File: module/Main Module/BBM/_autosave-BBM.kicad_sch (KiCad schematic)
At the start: 27 parts, among them Q1 NPN, Q2 BS250, Q3 BS170, SW1 SW_DPDT_x2

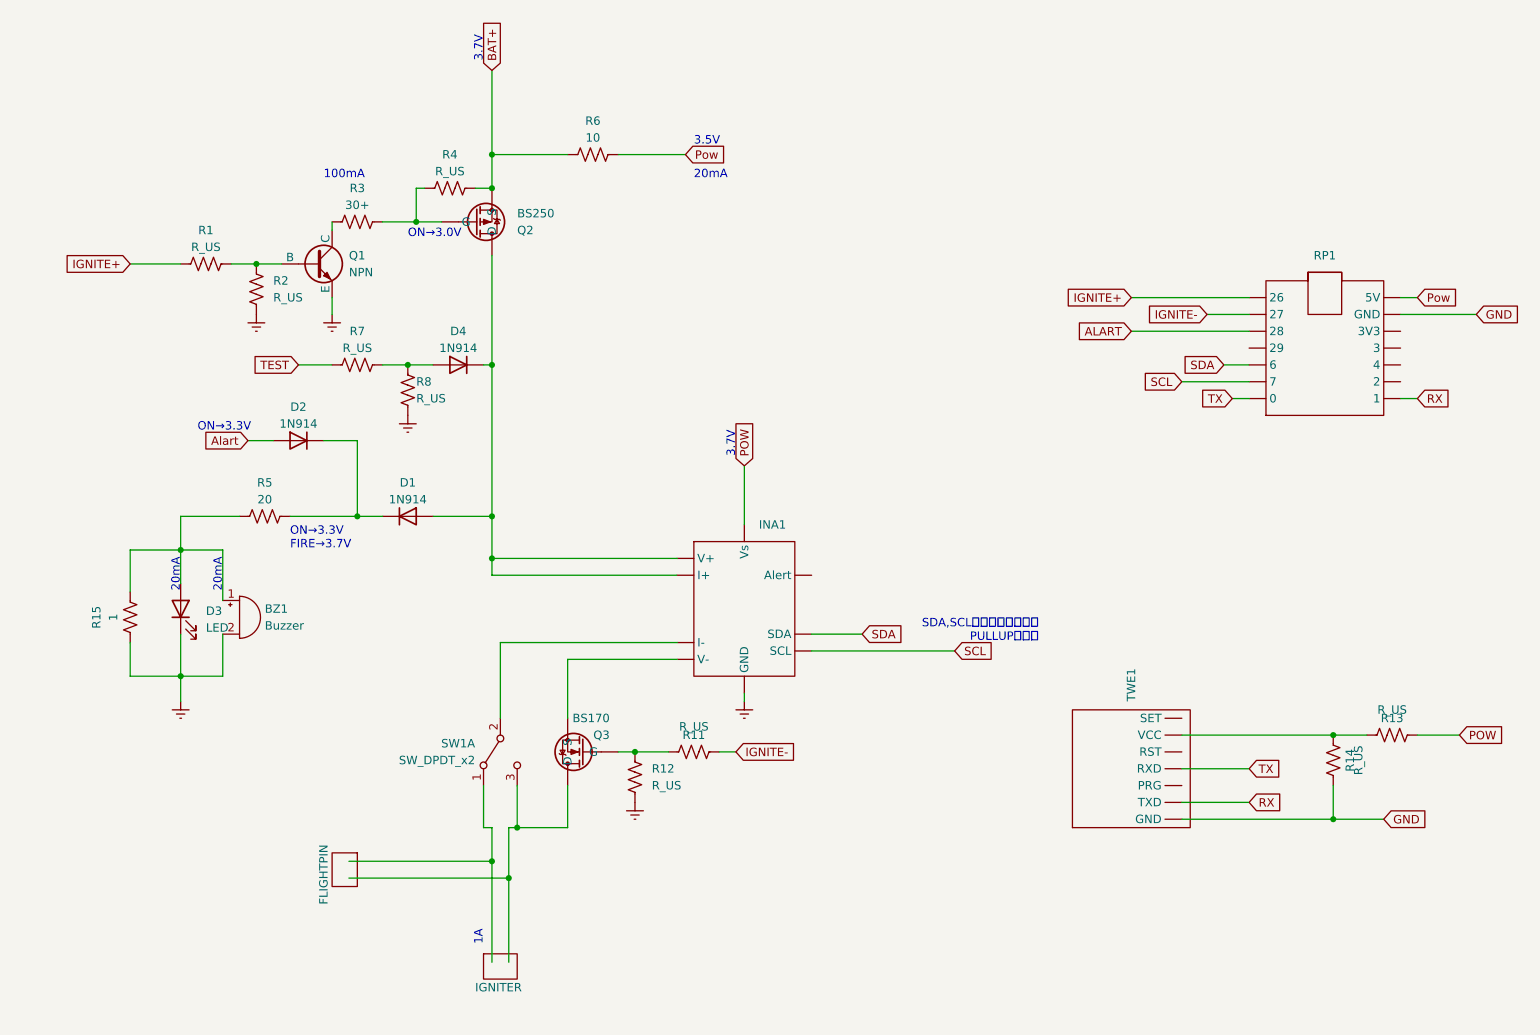
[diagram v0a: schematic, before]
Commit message: BBMに最適化したプログラム・回路を作りました
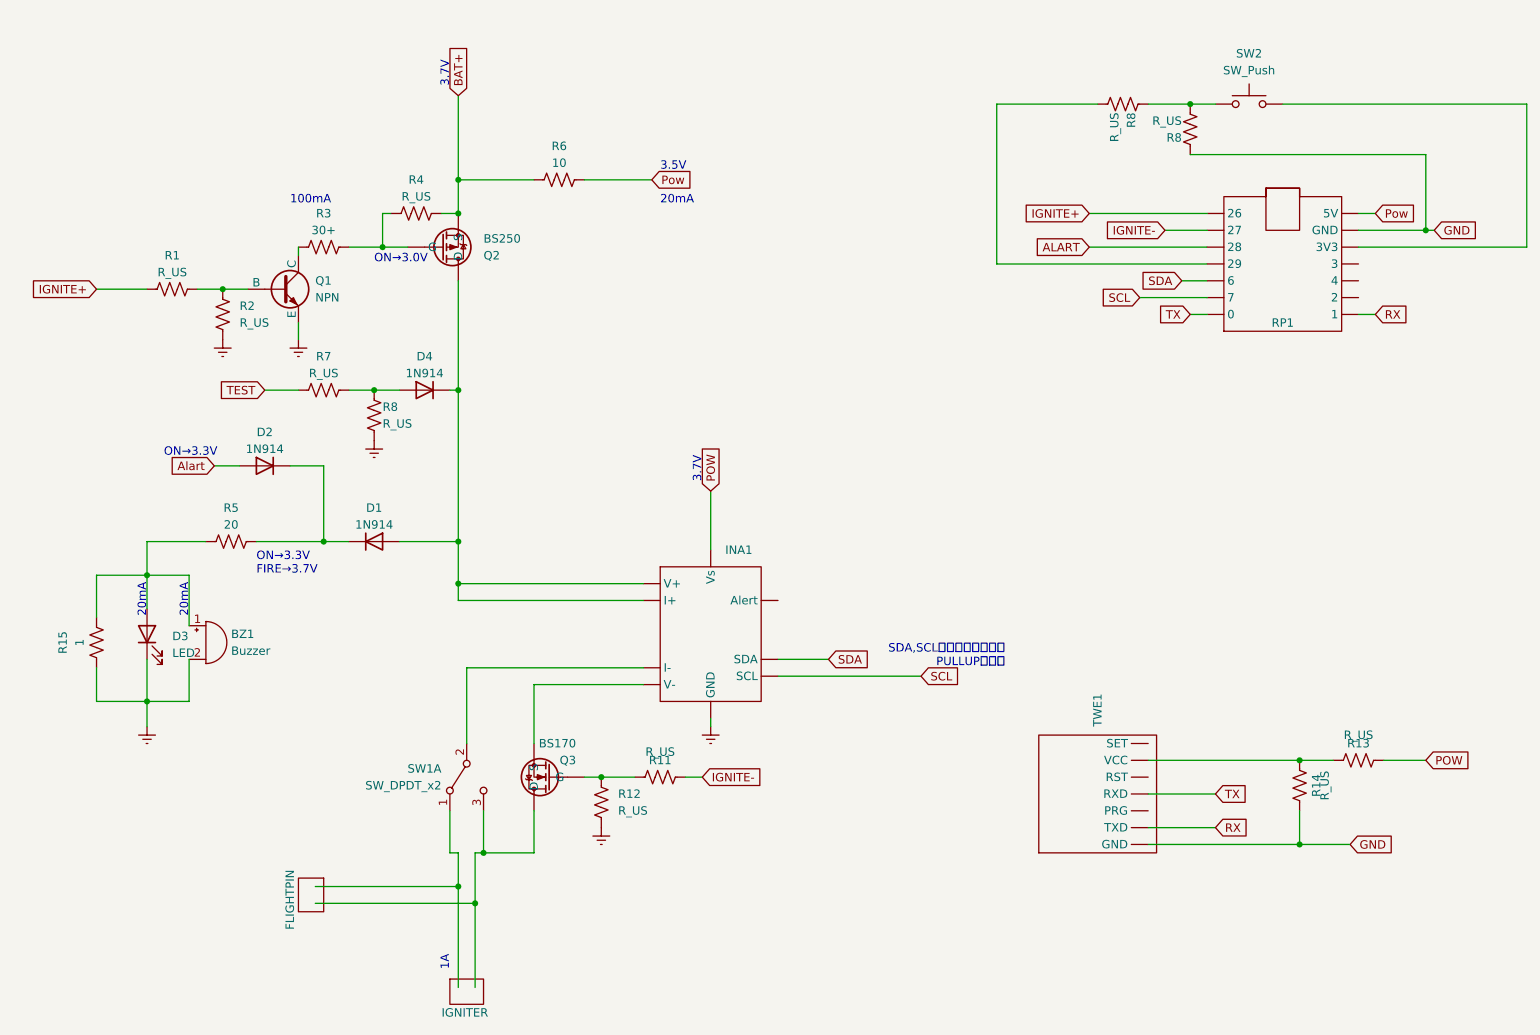
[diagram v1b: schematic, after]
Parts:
- removed R8: R_US, symbol Device:R_US
- added R8 (x3): R_US, symbol Device:R_US
- added SW2: SW_Push, symbol Switch:SW_Push
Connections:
- net Earth: now also R8.2
- net GND: now also R8.1
- net at D4.2 (A), R7.1: now also R8.1
- new net: R8.1, R8.2, SW2.1
- new net: RP1. (GND), SW2.2
- new net: R8.2, RP1. (GND)
